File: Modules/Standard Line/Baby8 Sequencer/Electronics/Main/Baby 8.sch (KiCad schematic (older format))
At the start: 62 parts, among them J1 Power, J10 Gate 6, J11 Gate 7, J12 Gate 8, J2 CV Out, J3 CLK In, J4 Reset, J5 Gate 1, J6 Gate 2, J7 Gate 3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

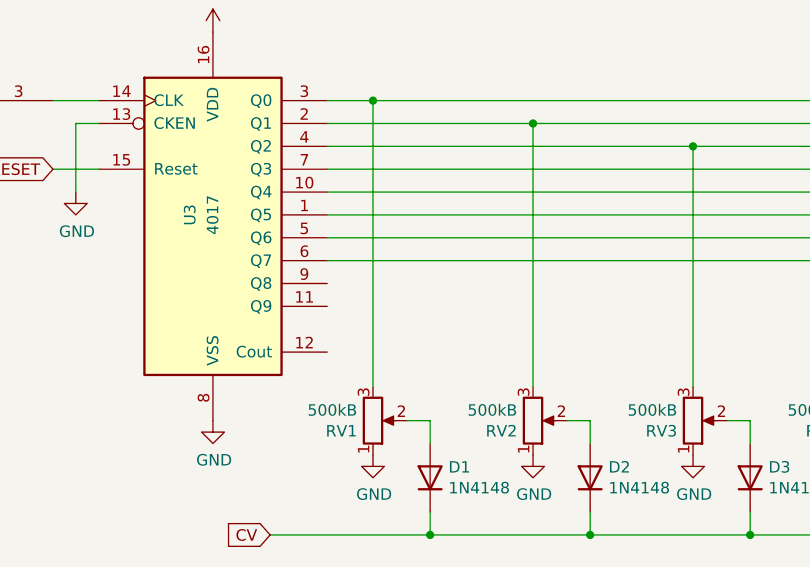
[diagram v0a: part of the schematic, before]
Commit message: 4Ch Mixer added
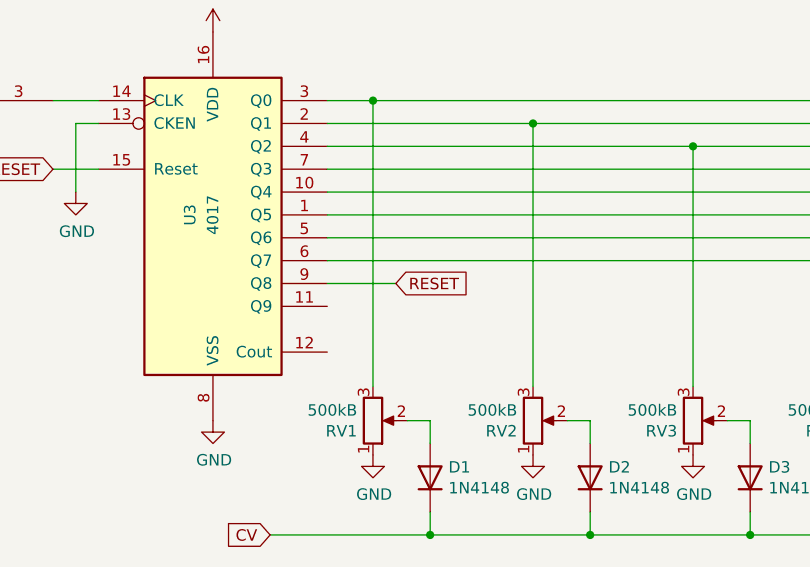
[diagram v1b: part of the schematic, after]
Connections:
- net RESET: now also U3.9 (Q8)
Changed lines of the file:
@@
 EELAYER 30 0
 EELAYER END
-$Descr A4 11693 8268
+$Descr A2 23386 16535
 encoding utf-8
 Sheet 1 1
@@
 	1    0    0    1
 $EndComp
+Text GLabel 5950 1950 2    50   Input ~ 0
+RESET
+Wire Wire Line
+	5650 1950 5950 1950
 $EndSCHEMATC
